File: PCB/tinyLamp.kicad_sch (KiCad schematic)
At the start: 54 parts, among them J1 USB_B_Mini, J2 Conn_02x03_Odd_Even, Q1 Q_NPN_BCE, Q2 Q_NPN_BCE, Q3 Q_NPN_BCE, Q4 Q_NPN_BCE, SW1 SW_Push, SW2 SW_Push, SW3 SW_Push, SW4 SW_Push, U1 TP4056, U2 ATtiny13A-SS, X1 BATT+, X2 BATT-

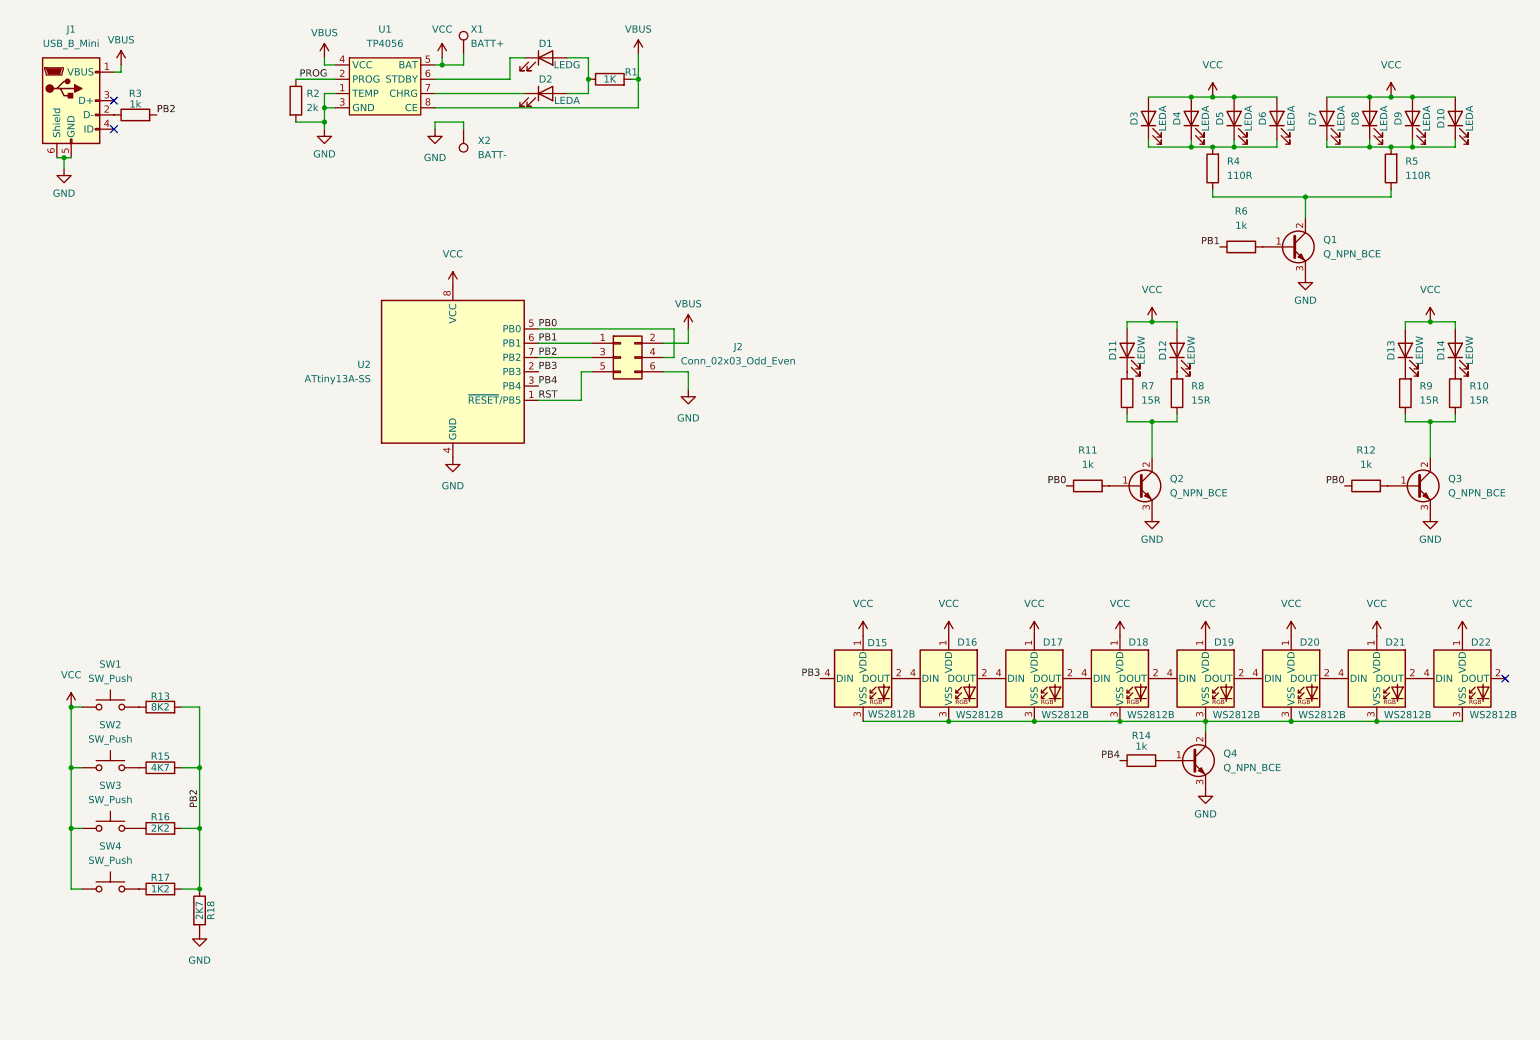
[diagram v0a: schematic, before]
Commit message: switches are using rst pin
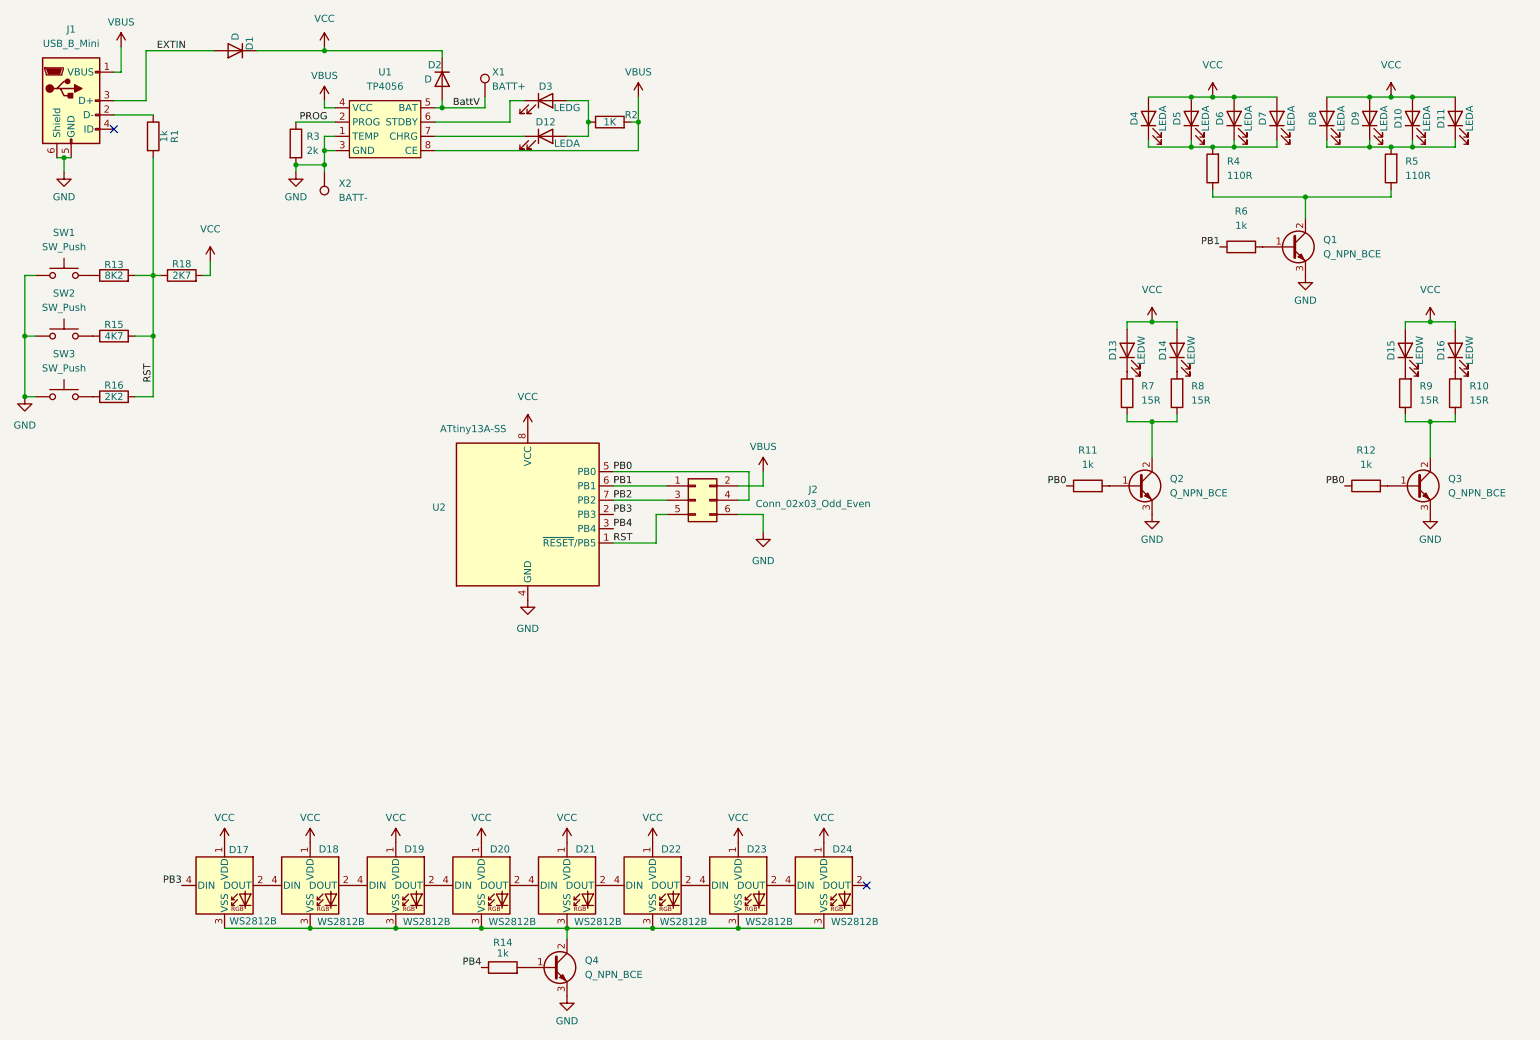
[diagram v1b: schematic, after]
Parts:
- removed R17: 1K2, Resistor_SMD:R_1206_3216Metric_Pad1.30x1.75mm_HandSolder, symbol Device:R
- removed SW4: SW_Push, Button_Switch_SMD:SW_SPST_CK_RS282G05A3, symbol Switch:SW_Push
- added D1: D, Diode_SMD:D_1206_3216Metric_Pad1.42x1.75mm_HandSolder, symbol Device:D
- added D2: D, Diode_SMD:D_SOD-123, symbol Device:D
- renumbered D9 to D10, D10 to D11, D2 to D12, D11 to D13, D12 to D14, D13 to D15, D14 to D16, D15 to D17, D16 to D18, D17 to D19, D18 to D20, D19 to D21, D20 to D22, D21 to D23, D22 to D24, D1 to D3, D3 to D4, D4 to D5, D5 to D6, D6 to D7, D7 to D8, D8 to D9, R3 to R1, R1 to R2, R2 to R3
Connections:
- net GND: now also SW1.1, SW2.1, SW3.1; no longer R18.2
- net PB2: no longer R1.2, R13.2, R15.2, R16.2, R18.1
- net RST: now also R1.2, R13.2, R15.2, R16.2, R18.1
- net VCC: now also R18.2, D1.1 (K), D2.1 (K); no longer SW1.1, SW2.1, SW3.1, U1.5 (BAT), X1.1
- net EXTIN: now reaches J1.3 (D+)
- net EXTIN: now also D1.2 (A)
- new net BattV: D2.2 (A), U1.5 (BAT), X1.1
- no-connect marks 3 -> 2
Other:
- moved on the sheet: D12, D17, D18, D19, D20, D21, D22, D23, D24, D3, J2, Q4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

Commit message: made Sub schematics
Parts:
- removed D10, D11, D4, D5, D6, D7, D8, D9: LEDA, LED_SMD:LED_0805_2012Metric_Pad1.15x1.40mm_HandSolder, symbol Device:LED
- removed D13, D14, D15, D16: LEDW, LED_SMD:LED_PLCC-2, symbol Device:LED
- removed D17, D18, D19, D20, D21, D22, D23, D24: WS2812B, LED_SMD:LED_WS2812B_PLCC4_5.0x5.0mm_P3.2mm, symbol LED:WS2812B
- removed D2: D, Diode_SMD:D_SOD-123, symbol Device:D
- removed Q1, Q2, Q3, Q4: Q_NPN_BCE, Package_TO_SOT_SMD:SOT-23, symbol Device:Q_NPN_BCE
- removed R10, R7, R8, R9: 15R, Resistor_SMD:R_1206_3216Metric_Pad1.30x1.75mm_HandSolder, symbol Device:R
- removed R11, R12, R6: 1k, Resistor_SMD:R_1206_3216Metric_Pad1.30x1.75mm_HandSolder, symbol Device:R
- removed R13: 8K2, Resistor_SMD:R_1206_3216Metric_Pad1.30x1.75mm_HandSolder, symbol Device:R
- removed R15: 4K7, Resistor_SMD:R_1206_3216Metric_Pad1.30x1.75mm_HandSolder, symbol Device:R
- removed R16: 2K2, Resistor_SMD:R_1206_3216Metric_Pad1.30x1.75mm_HandSolder, symbol Device:R
- removed R18: 2K7, Resistor_SMD:R_1206_3216Metric_Pad1.30x1.75mm_HandSolder, symbol Device:R
- removed R4, R5: 110R, Resistor_SMD:R_1206_3216Metric_Pad1.30x1.75mm_HandSolder, symbol Device:R
- removed U2: ATtiny13A-SS, Package_SO:SOIC-8_3.9x4.9mm_P1.27mm, symbol MCU_Microchip_ATtiny:ATtiny13A-SS
- added Q11: Q_PNP_BCE, Package_TO_SOT_SMD:SOT-23, symbol Device:Q_PNP_BCE
- added U12: ATtiny24A-SS, Package_SO:SOIC-14_3.9x8.7mm_P1.27mm, symbol MCU_Microchip_ATtiny:ATtiny24A-SS
- D11: renamed from D1; footprint Diode_SMD:D_1206_3216Metric_Pad1.42x1.75mm_HandSolder -> Diode_SMD:D_SOD-123
- R14: value 1k -> 12k; Price 0.0021 -> (none)
- renumbered D3 to D12, D12 to D13, J1 to J11, J2 to J12, R1 to R11, R2 to R12, R3 to R13, SW1 to SW11, SW2 to SW12, SW3 to SW13, U1 to U11, X1 to X11, X2 to X12
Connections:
- net BattV is gone; now on net VCC: U11.5 (BAT), X11.1
- net GND: now also SW11.2, SW12.2, SW13.2, U12.14 (GND); no longer SW11.1, SW12.1, SW13.1
- net RST: now also U12.4 (~{RESET}/PB3); no longer R11.2
- net VCC: now also D11.2 (A), Q11.3 (E), U12.1 (VCC); no longer D11.1 (K)
- net at R14.2: now also Q11.1 (B)
- net EXTIN renamed EXTOUT
- net EXTOUT: now also D11.1 (K); no longer D11.2 (A)
- net PB0 renamed MOSI_PWM2
- net MOSI_PWM2: now also U12.7 (PA6)
- net PB1 renamed MISO_PWM3
- net MISO_PWM3: now also U12.8 (PA5)
- net PB2 renamed SCK
- net SCK: now also U12.9 (PA4)
- net PB4 renamed LEDR_EN
- net LEDR_EN: now also U12.3 (XTAL2/PB1)
- new net INT3_DATA: R11.2, U12.10 (PA3)
- new net LEDA_EN: U12.2 (XTAL1/PB0)
- new net PWM0: U12.5 (PB2)
- new net PWM1: U12.6 (PA7)
- new net PWRSW: SW11.1, U12.13 (AREF/PA0)
- new net RGBleds/LEDR_VCC: Q11.2 (C)
- new net SW_M: SW13.1, U12.11 (PA2)
- new net SW_P: SW12.1, U12.12 (PA1)
- no-connect marks 2 -> 1
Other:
- added sheet RGBleds (RGBleds.kicad_sch)
- added sheet ledO (ledO.kicad_sch)
- added sheet ledW (ledW.kicad_sch)
- note added: "LEDs"
- note added: "Power"
- moved on the sheet: D11, D12, D13, J11, J12, R11, R12, R13, SW11, SW12, SW13, U11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

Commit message: made some Changes
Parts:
- removed Q11: Q_PNP_BCE, Package_TO_SOT_SMD:SOT-23, symbol Device:Q_PNP_BCE
- removed R12: 1K, Resistor_SMD:R_1206_3216Metric_Pad1.30x1.75mm_HandSolder, symbol Device:R
- removed R14: 12k, Resistor_SMD:R_1206_3216Metric_Pad1.30x1.75mm_HandSolder, symbol Device:R
- added R13: 1k, Resistor_SMD:R_1206_3216Metric_Pad1.30x1.75mm_HandSolder, symbol Device:R
- added R? (x5): R, symbol Device:R
- renumbered R11 to R12, R13 to R14
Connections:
- net LEDA_EN: now also R?.2
- net LEDR_EN: now also R?.2
- net MISO_PWM3: now also R?.1
- net MOSI_PWM2: now also R?.1, R?.1
- net PWM0: now also R?.1
- net PWM1: now also R?.1
- net VBUS: now also R13.2
- net at D12.2 (A), D13.2 (A): now also R13.1
- new net RGBleds/LEDG: R?.2
- new net RGBleds/LEDR: R?.2
- new net ledW/LEDW: R?.2
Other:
- sheet RGBleds ports: added LEDB, LEDG, LEDR; removed LEDB_IN, LEDB_VCC, LEDG_IN, LEDG_VCC, LEDR_IN, LEDR_VCC
- sheet ledO ports: added LEDA; removed LEDA_D, LEDA_EN

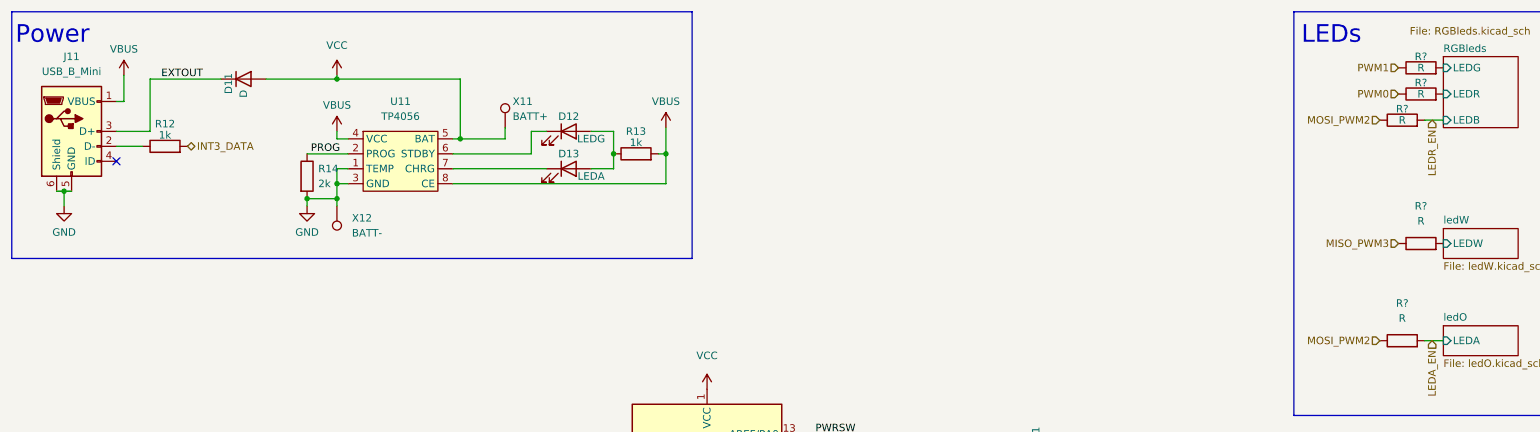
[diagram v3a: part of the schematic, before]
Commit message: added Capacitor and updated PCB
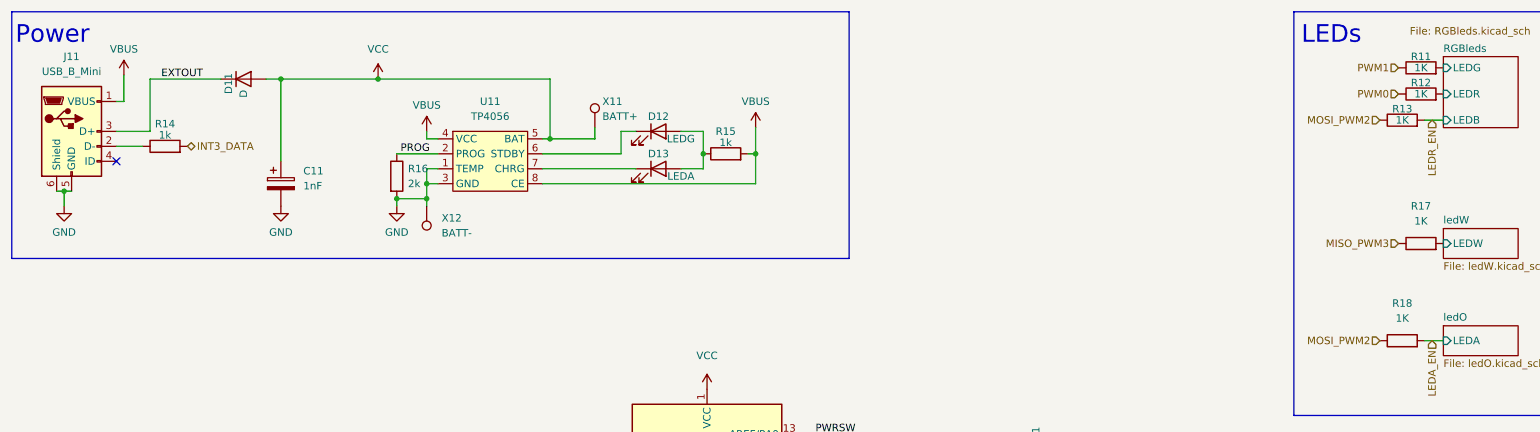
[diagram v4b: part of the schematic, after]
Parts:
- added C11: 1nF, Capacitor_SMD:C_1206_3216Metric_Pad1.33x1.80mm_HandSolder, symbol Device:C_Polarized
- R11, R12, R13, R17, R18: renamed from R?; value R -> 1K; footprint (none) -> Resistor_SMD:R_1206_3216Metric_Pad1.30x1.75mm_HandSolder
- renumbered R12 to R14, R13 to R15, R14 to R16
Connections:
- net GND: now also C11.2
- net VCC: now also C11.1
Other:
- moved on the sheet: D12, D13, R15, R16, U11, X11, X12
